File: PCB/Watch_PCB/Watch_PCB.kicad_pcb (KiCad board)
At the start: 2 copper layers, 30 x 30 mm, 71 parts, among them IC1 PCF2003DUS, IC2 BMM350, IC3 STM32L011E4Y6TR, Q1 2N7002KQBZ, Q1 NMOS, Q10 2N7002KQBZ, Q11 2N7002KQBZ, Q12 2N7002KQBZ, Q2 BSS84AKQBZ, Q2 PMOS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

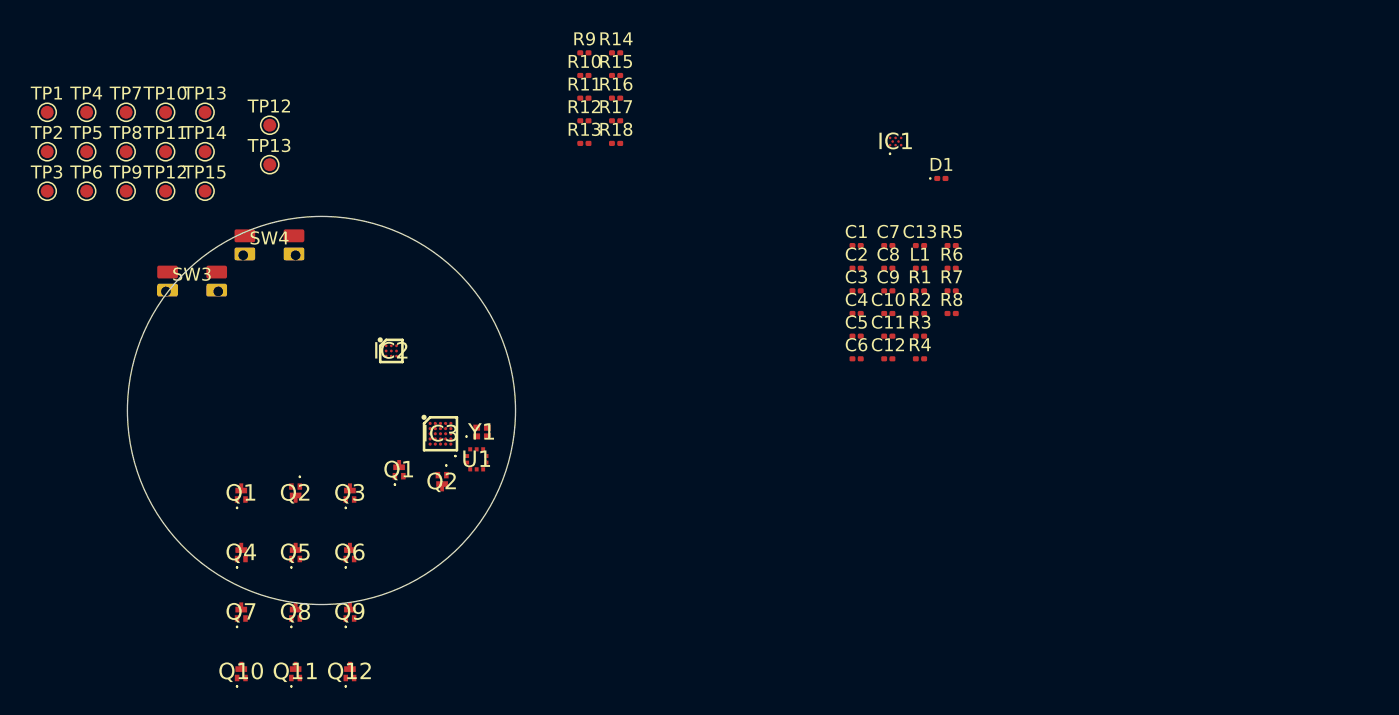
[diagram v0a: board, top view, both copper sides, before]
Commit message: pcb outline
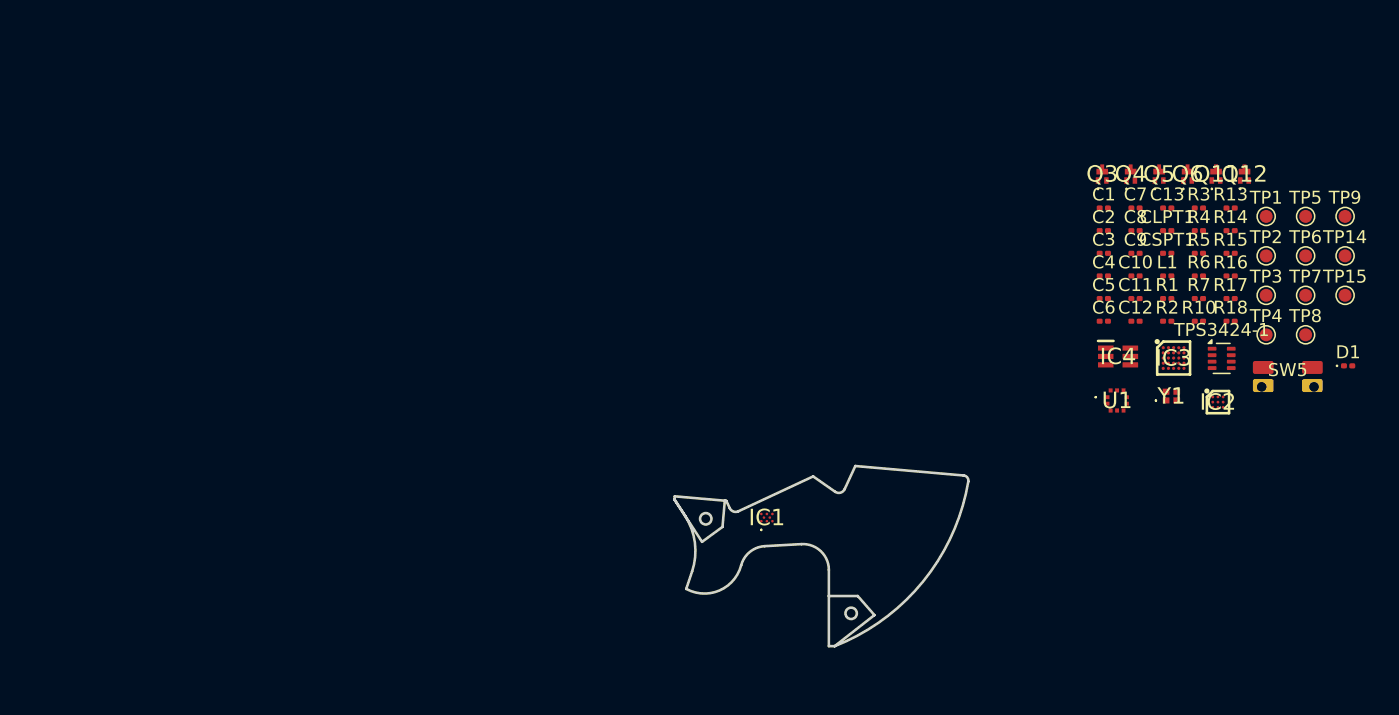
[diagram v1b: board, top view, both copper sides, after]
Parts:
- removed Q1: NMOS, SamacSys_Parts:2N7002KQBZ
- removed Q1, Q10, Q7, Q8, Q9: 2N7002KQBZ, SamacSys_Parts:2N7002KQBZ
- removed Q2: BSS84AKQBZ, SamacSys_Parts:BC81725QBZ
- removed Q2: PMOS, SamacSys_Parts:BC81725QBZ
- removed R11, R12, R9: 100k, Resistor_SMD:R_0201_0603Metric
- removed R8: 1M, Resistor_SMD:R_0201_0603Metric
- removed SW3, SW4: SW_MEC_5E, SamacSys_Parts:Wurth side button 434331013822
- removed TP10, TP12: SD2+, TestPoint:TestPoint_Pad_D1.0mm
- removed TP11, TP13: SD2-, TestPoint:TestPoint_Pad_D1.0mm
- removed TP12: SD3+, TestPoint:TestPoint_Pad_D1.0mm
- removed TP13: SD_3-, TestPoint:TestPoint_Pad_D1.0mm
- added CLPT1: 1u, Capacitor_SMD:C_0201_0603Metric, F.Cu at (130.4, 86.1)
- added CSPT1: 1u, Capacitor_SMD:C_0201_0603Metric, F.Cu at (130.4, 87.8)
- added IC4: TPS22919DCKR, SamacSys_Parts:SOT65P210X110-6N, F.Cu at (126.6, 95.8)
- added SW5: SW_MEC_5E, SamacSys_Parts:Wurth side button 434331013822, F.Cu at (139.7, 97.4)
- added TPS3424-1: ~, Package_TO_SOT_SMD:SOT-583-8, F.Cu at (134.6, 96.0)
- C12: value 1n -> 220n
- R17: value 100k -> 1k
- R18: value 100k -> 47k
- moved TP1 94.6 mm to (138.0, 85.0)
- moved TP2 94.6 mm to (138.0, 88.0)
- moved TP3 94.6 mm to (138.0, 91.1)
- moved TP5 94.4 mm to (141.1, 85.0)
- moved TP6 94.4 mm to (141.1, 88.0)
- moved TP9 94.2 mm to (144.1, 85.0)
- moved TP4 92.8 mm to (138.0, 94.2)
- moved TP7 92.3 mm to (141.1, 91.1)
- moved TP8 92.3 mm to (141.1, 94.2)
- moved TP14 88.5 mm to (144.1, 88.0)
- moved TP15 88.5 mm to (144.1, 91.1)
- moved Q11 80.9 mm to (134.2, 81.7)
- moved Q12 79.1 mm to (136.3, 81.7)
- moved Q4 74.7 mm to (127.5, 81.7)
- moved Q5 72.9 mm to (129.8, 81.7)
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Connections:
- C1 pad 2: Monostable output -> Controller Output
- C12 pad 1: GPIO_EXTI1 -> GND
- C12 pad 2: Net-(Q1-D_1) -> Net-(SW5-A)
- C2 pad 2: Monostable output -> Controller Output
- IC3 pad D1: Monostable output -> Controller Output
- IC3 pad D2: Tim2_CH4 -> unconnected-(IC3-PB1-PadD2)
- IC3 pad E2: Tim2_CH2 -> unconnected-(IC3-PB0-PadE2)
- L1 pad 1: Monostable output -> Controller Output
- R17 pad 1: Tim2_CH2 -> GND
- R17 pad 2: +3V0 -> Net-(SW5-A)
- R18 pad 1: +3V0 -> Net-(SW5-A)
- R18 pad 2: Tim2_CH4 -> GPIO_EXTI9
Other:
- board size 30 x 30 mm -> 22.7 x 13.9 mm

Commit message: pcb layout
pcb layout
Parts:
- removed Q11, Q12: 2N7002KQBZ, SamacSys_Parts:2N7002KQBZ
- removed R6, R7: 2k, Resistor_SMD:R_0201_0603Metric
- removed TP1: GND_PCF2003, TestPoint:TestPoint_Pad_D1.0mm
- removed TP14: B+, TestPoint:TestPoint_Pad_D1.0mm
- removed TP15: B-, TestPoint:TestPoint_Pad_D1.0mm
- removed TP2: VDD_PCF2003, TestPoint:TestPoint_Pad_D1.0mm
- removed TP3, TP4: MOT, TestPoint:TestPoint_Pad_D1.0mm
- removed TP5: SWDIO, TestPoint:TestPoint_Pad_D1.0mm
- removed TP6: SWCLK, TestPoint:TestPoint_Pad_D1.0mm
- removed TP7: NRST, TestPoint:TestPoint_Pad_D1.0mm
- removed TP8: SD1+, TestPoint:TestPoint_Pad_D1.0mm
- removed TP9: SD1-, TestPoint:TestPoint_Pad_D1.0mm
- IC4: value TPS22919DCKR -> TPS22991BRAAR; footprint SamacSys_Parts:SOT65P210X110-6N -> SamacSys_Parts:TPS22991BRAAR
- moved D1 62.5 mm to (82.3, 88.9), turned to -77 degrees
- moved Y1 51.2 mm to (80.6, 88.2), turned to -165 degrees
- moved R3 50.6 mm to (82.6, 90.7), turned to -77 degrees
- moved R2 49.4 mm to (81.0, 91.1), turned to 103 degrees
- moved IC2 48.7 mm to (86.1, 92.4), turned to 141 degrees
- moved R1 48.6 mm to (81.8, 90.9), turned to -77 degrees
- moved R5 44.7 mm to (88.4, 92.7), turned to -39 degrees
- moved R13 44.6 mm to (90.8, 88.0), turned to 90 degrees
- moved R4 43.8 mm to (89.5, 92.7), turned to -39 degrees
- moved C9 43.7 mm to (84.4, 91.8), turned to 141 degrees
- moved R15 43.6 mm to (91.7, 89.5), turned to -90 degrees
- moved SW5 41.8 mm to (98.2, 92.3), turned to 115 degrees
- moved C11 40.9 mm to (87.1, 93.2), turned to 50 degrees
- moved R14 40.6 mm to (94.7, 86.0), turned to 135 degrees
- moved C5 40.6 mm to (84.9, 91.2), turned to 141 degrees
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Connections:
- C11 pad 2: CompVCC -> Controller Output
- C12 pad 2: Net-(SW5-A) -> Net-(C12-Pad2)
- C5 pad 1: BaroVCC -> Controller Output
- C9 pad 1: BaroVCC -> Controller Output
- IC2 pad B3: BaroVCC -> Controller Output
- IC2 pad C1: BaroVCC -> Controller Output
- IC4 pad 2: GND -> Net-(IC4-ON)
- IC4 pad 3: Net-(IC4-ON) -> Controller Output
- IC4 pad 4: unconnected-(IC4-N/C-Pad4) -> GND
- R17 pad 2: Net-(SW5-A) -> Net-(C12-Pad2)
- R18 pad 1: Net-(SW5-A) -> Net-(C12-Pad2)
- R4 pad 1: BaroVCC -> Controller Output
- R5 pad 1: BaroVCC -> Controller Output
- SW5 pad 1: +3V0 -> Net-(C12-Pad2)
- SW5 pad 2: +3V0 -> Net-(C12-Pad2)
- SW5 pad 3: Net-(SW5-A) -> +3V0
- SW5 pad 4: Net-(SW5-A) -> +3V0
- U1 pad 10: CompVCC -> Controller Output
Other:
- outline, holes or cut-outs redrawn
- copper layers 2 -> 8

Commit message: PCB V1
PCB V1 complete
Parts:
- added L2: L, SamacSys_Parts:Miyota 2035, B.Cu at (92.1, 85.6)
- added L3: L, SamacSys_Parts:Miyota 2035, B.Cu at (80.8, 92.9)
- added TP1: GND_PCF2003, TestPoint:TestPoint_Pad_D1.0mm, B.Cu at (80.8, 90.6)
- added TP14: B+, TestPoint:TestPoint_Pad_D1.0mm, B.Cu at (96.6, 88.8)
- added TP15: B-, TestPoint:TestPoint_Pad_D1.0mm, B.Cu at (98.9, 92.0)
- added TP2: VDD_PCF2003, TestPoint:TestPoint_Pad_D1.0mm, B.Cu at (82.5, 88.8)
- added TP5: SWDIO, TestPoint:TestPoint_Pad_D1.0mm, B.Cu at (92.2, 91.2)
- added TP6: SWCLK, TestPoint:TestPoint_Pad_D1.0mm, B.Cu at (93.2, 93.0)
- added TP7: NRST, TestPoint:TestPoint_Pad_D1.0mm, B.Cu at (94.3, 91.2)
- moved D1 13.5 mm to (95.8, 89.3), turned to 45 degrees
- moved R10 0.29 mm to (92.5, 95.2)
- moved CSPT1 0.20 mm to (94.4, 93.9)
- moved Y1 0.15 mm to (80.5, 88.1), turned to 15 degrees
- moved Q4 0.11 mm to (93.7, 86.8)
- moved C5 0.11 mm to (84.8, 91.3)
- moved Q3 0.10 mm to (92.1, 88.0)
- moved C9 0.09 mm to (84.3, 91.9)
- moved C7 0.08 mm to (88.3, 91.7)
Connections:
- Y1 pad 4: unconnected-(Y1-NC-Pad4) -> GND
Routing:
- net Controller Output: track 0.00 -> 25.1 mm, vias 0 -> 5
- net Tim2_CH3: track 0.00 -> 12.5 mm, vias 0 -> 3
- net I2C1_SCL: track 0.00 -> 12.5 mm, vias 0 -> 4
- net I2C1_SDA: track 0.00 -> 10.5 mm, vias 0 -> 4
- net Tim2_CH1: track 0.00 -> 10.2 mm, vias 0 -> 3
- net GPIO_EXTI1: track 0.00 -> 6.24 mm, vias 0 -> 2
- net Net-(IC3-VDDA): track 0.00 -> 5.87 mm, vias 0 -> 2
- net GPIO_EXTI9: track 0.00 -> 5.79 mm, vias 0 -> 2
- net GPIO_Output_Mono: track 0.00 -> 5.53 mm, vias 0 -> 2
- net Net-(IC1-MOT1): track 0.00 -> 5.34 mm, vias 0 -> 2
- net Net-(Q3-D_1): track 0.00 -> 5.26 mm, vias 0 -> 1
- net Net-(IC1-MOT2): track 0.00 -> 4.21 mm, vias 0 -> 2
- net NRST: track 0.00 -> 3.63 mm, vias 0 -> 2
- net Net-(Q4-D_1): track 0.00 -> 3.61 mm, vias 0 -> 1
- net Net-(IC2-CRST): track 0.00 -> 3.20 mm
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- added copper zone on In3.Cu, net +3V0
- added copper zone on B.Cu, net GND
- added copper zone on F.Cu, net GND
- added copper zone on In1.Cu, net GND
- added copper zone on In2.Cu, net GND
- added copper zone on In4.Cu, net GND
- added copper zone on F.Cu, net Net-(C12-Pad2)
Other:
- copper layers 8 -> 6
